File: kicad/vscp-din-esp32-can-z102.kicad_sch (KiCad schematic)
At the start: 37 parts, among them J1 Conn_01x05, J2 Conn_01x02, J3 Conn_01x06, J4 Conn_01x04, J5 Conn_01x04, J6 Conn_01x03, J7 Conn_01x05, J8 Conn_01x02, U1 ESP32-C3-WROOM-02-N4, U2 LM2575-3.3BT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

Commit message: Rev B away for production
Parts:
- added D4: 1N5819, Diode_SMD:D_SOD-123, symbol Diode:1N5819
- added J9: Conn_01x02, Connector_PinHeader_2.54mm:PinHeader_1x02_P2.54mm_Vertical, symbol Connector_Generic:Conn_01x02
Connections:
- net +28V: now also D4.1 (K); no longer J5.1 (Pin_1)
- net GND: now also J9.1 (Pin_1)
- net reset: now also J9.2 (Pin_2)
- new net: D4.2 (A), J5.1 (Pin_1)

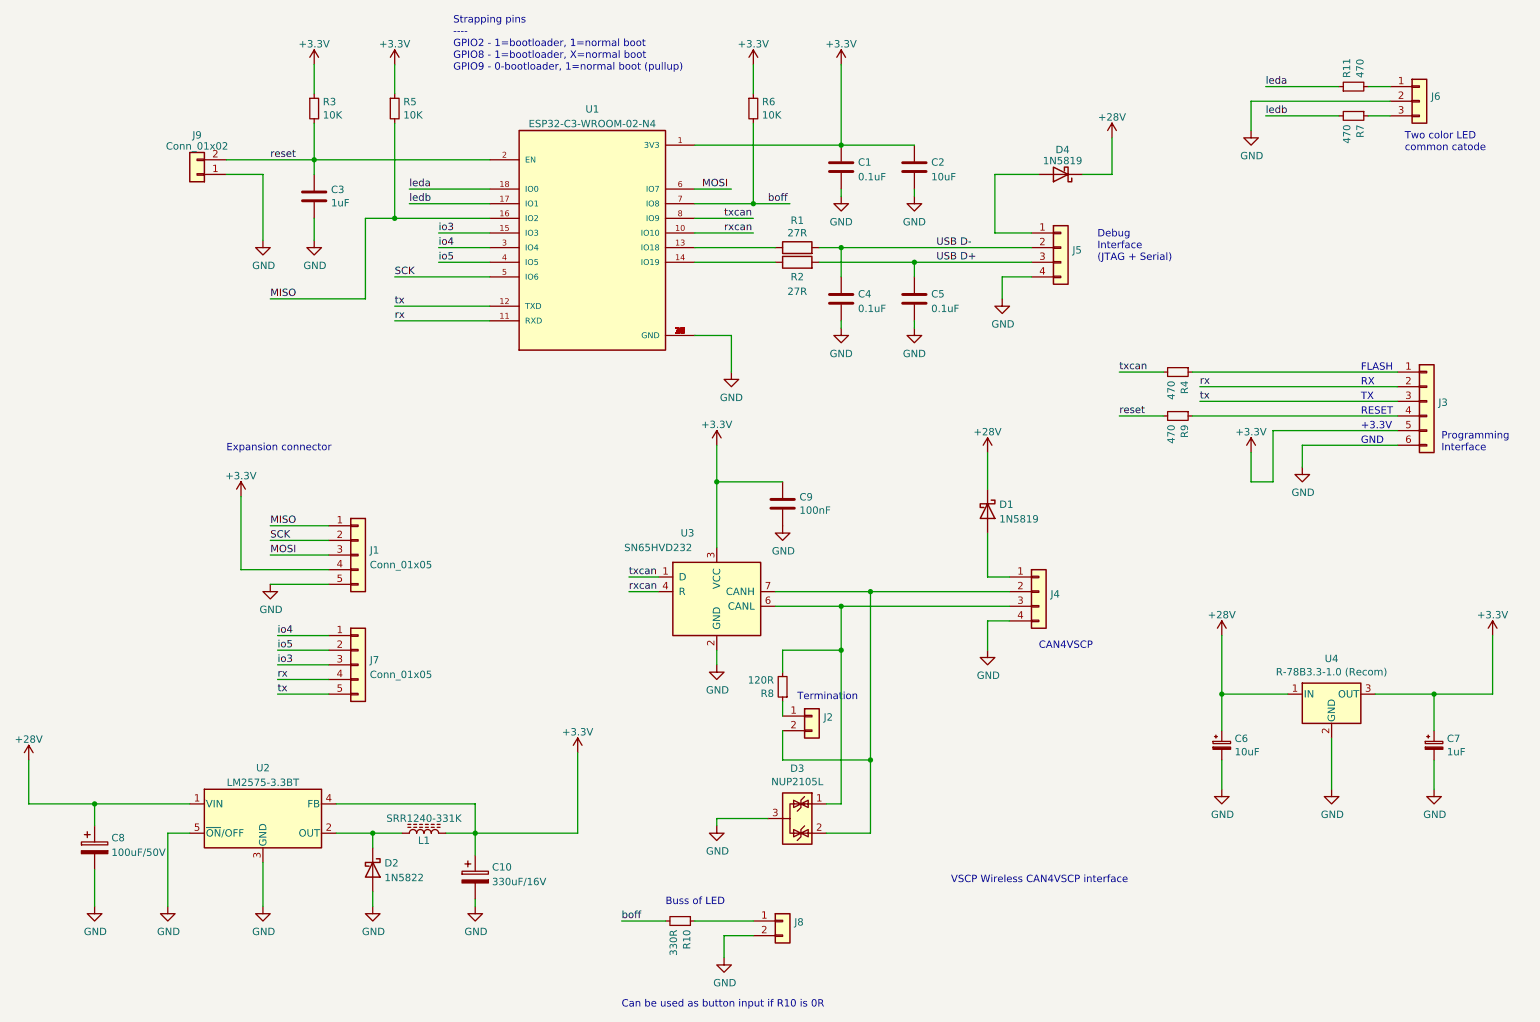
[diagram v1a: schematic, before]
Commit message: Updated schema to latest KiCAD
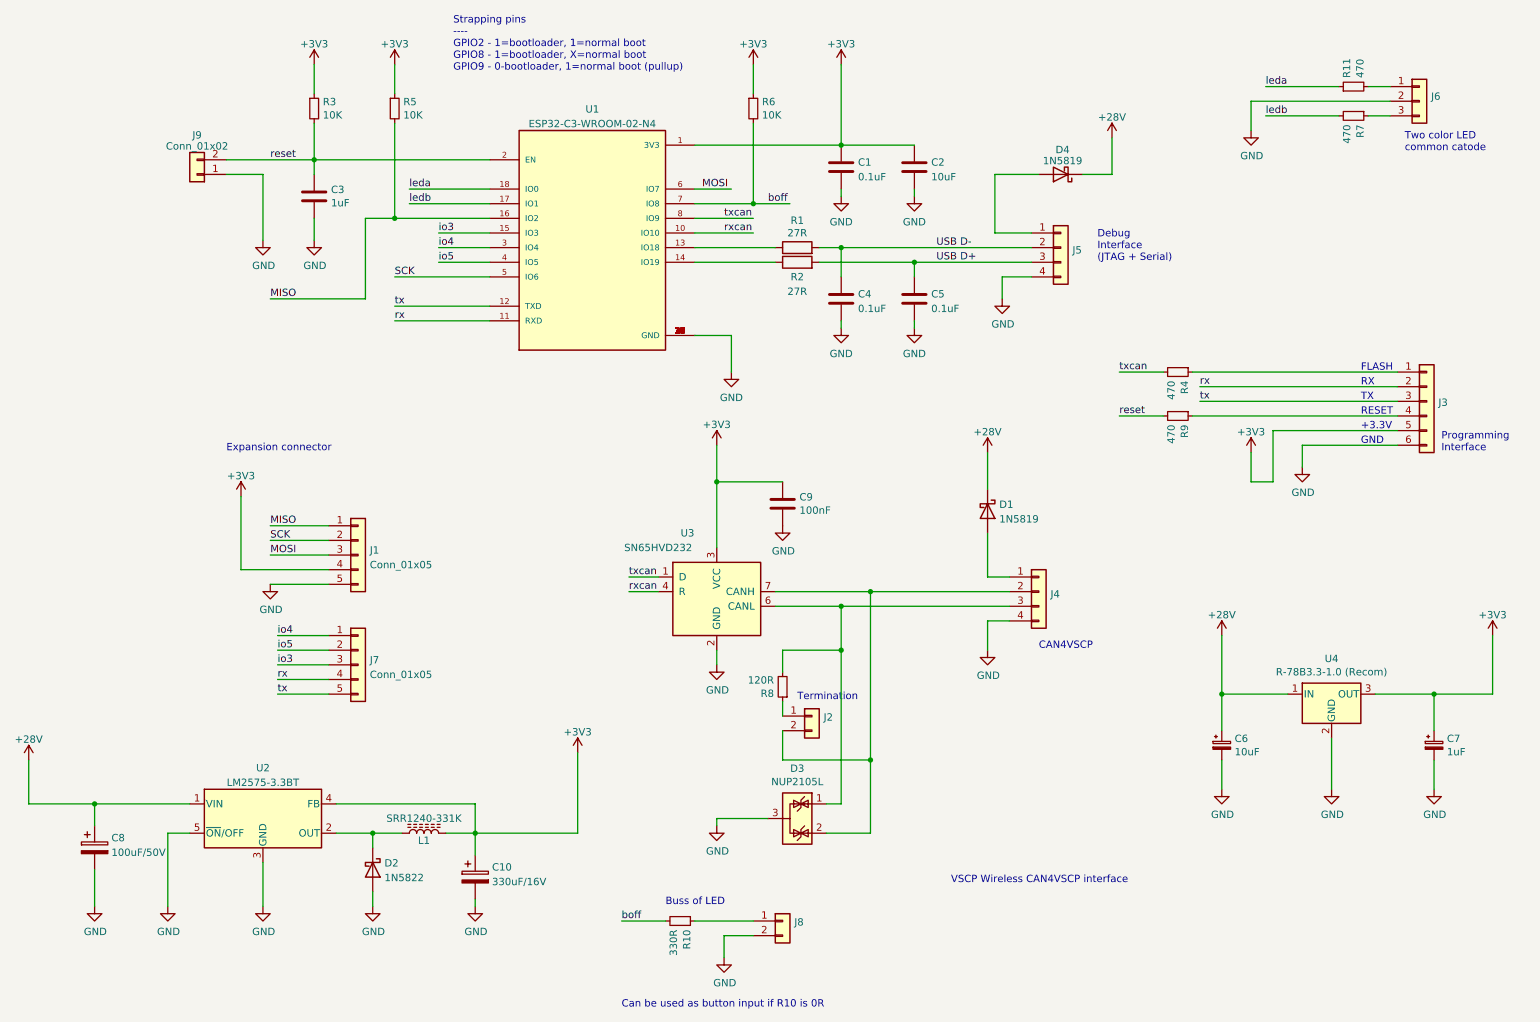
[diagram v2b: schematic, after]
